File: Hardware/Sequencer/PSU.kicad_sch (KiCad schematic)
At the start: 1 part, among them U601 AZ1117H-ADJ

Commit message: Régu
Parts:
- added C1, C2: 33nF, symbol Device:C
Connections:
- net GND: now also C1.2, C2.2

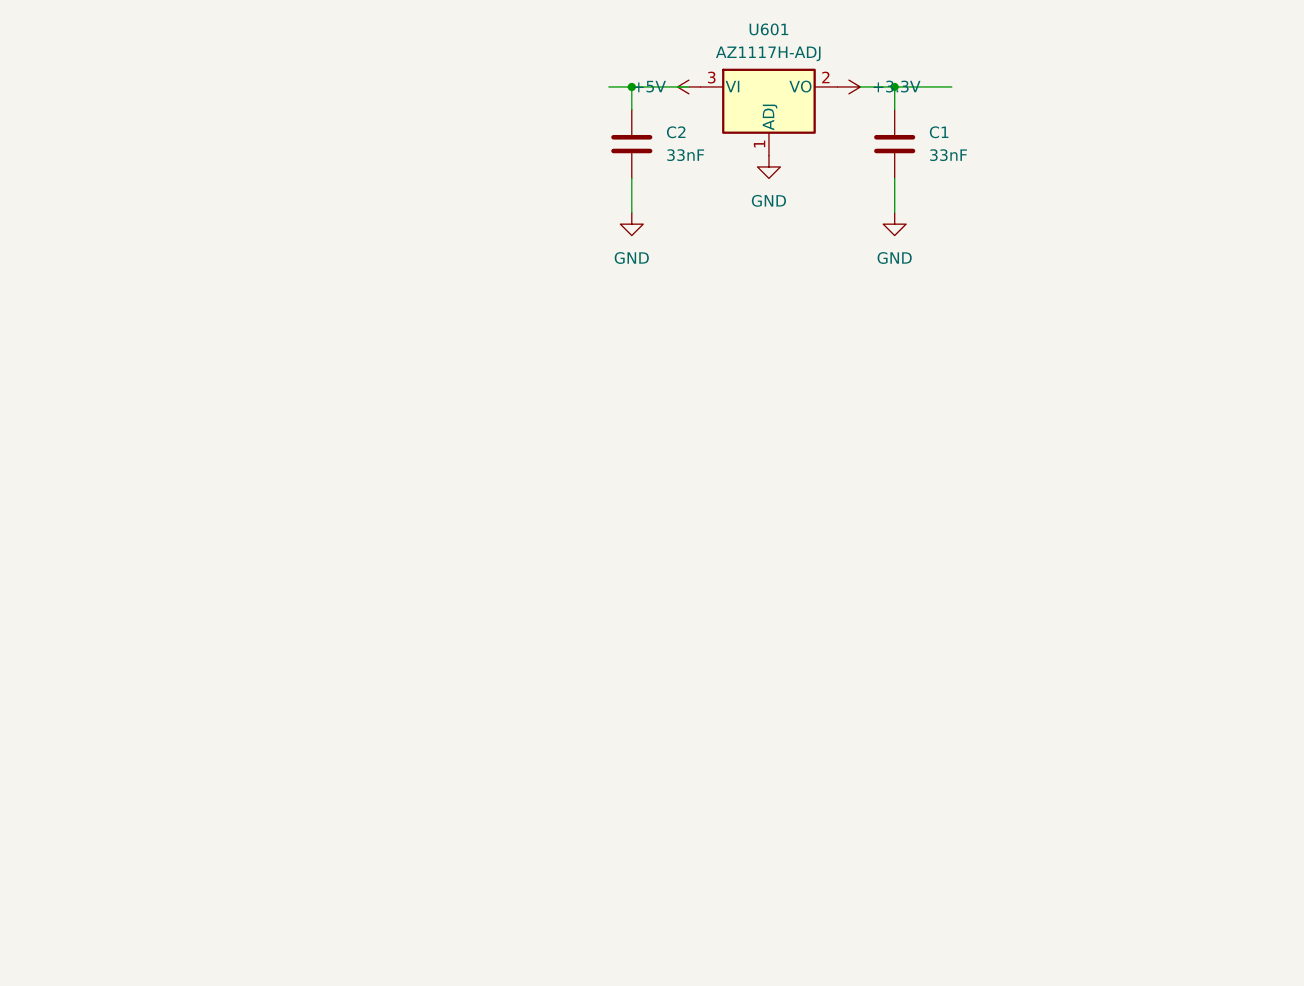
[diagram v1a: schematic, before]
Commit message: Beaucoup de changements sur le pcb
Alim corrigée, ajout de l'USB C

Sonde sur le processeur + linkage USB

Rajout des boutons (465M111...)
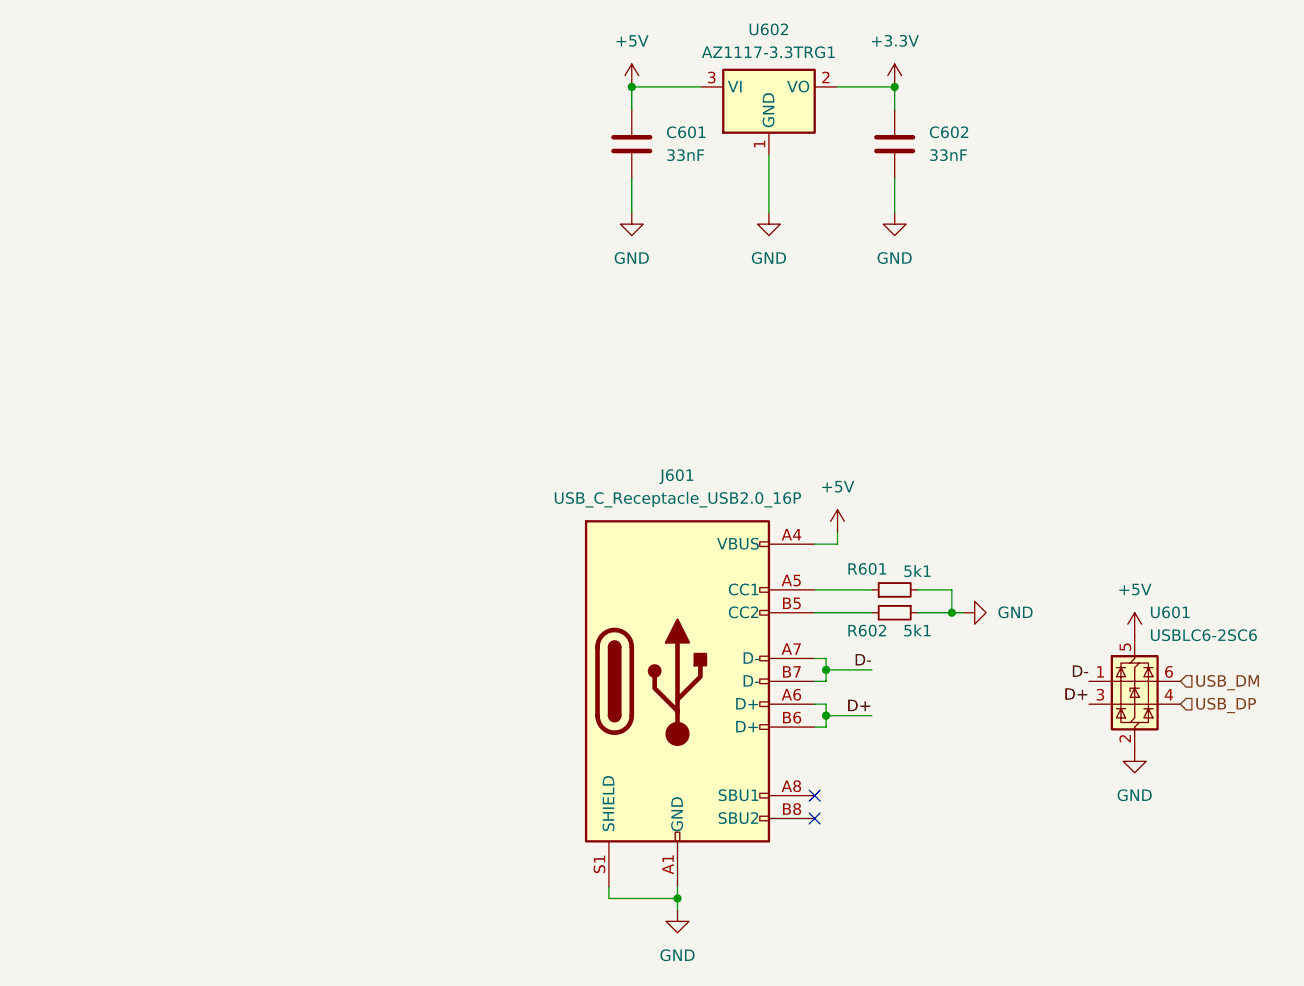
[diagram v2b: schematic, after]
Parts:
- removed U601: AZ1117H-ADJ, Package_TO_SOT_SMD:SOT-223-3_TabPin2, symbol Regulator_Linear:AZ1117H-ADJ
- added J601: USB_C_Receptacle_USB2.0_16P, Connector_USB:USB_C_Receptacle_HRO_TYPE-C-31-M-12, symbol Connector:USB_C_Receptacle_USB2.0_16P
- added R601, R602: 5k1, symbol Device:R_Small
- added U601: USBLC6-2SC6, Package_TO_SOT_SMD:SOT-223-3_TabPin2, symbol Power_Protection:USBLC6-2SC6
- added U602: AZ1117-3.3TRG1, Package_TO_SOT_SMD:SOT-223-3_TabPin2, symbol Regulator_Linear:AMS1117-3.3
- renumbered C2 to C601, C1 to C602
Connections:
- net +3.3V: now also C602.1, U602.2 (VO)
- net +5V: now also C601.1, J601.A4 (VBUS), J601.A9 (VBUS), J601.B4 (VBUS), J601.B9 (VBUS), U601.5 (VBUS), U602.3 (VI)
- net GND: now also J601.A1 (GND), J601.A12 (GND), J601.B1 (GND), J601.B12 (GND), J601.S1 (SHIELD), R601.2, R602.1, U601.2 (GND), U602.1 (GND)
- new net: J601.A5 (CC1), R601.1
- new net: J601.B5 (CC2), R602.2
- new net D+: J601.A6 (D+), J601.B6 (D+), U601.3 (I/O2)
- new net D-: J601.A7 (D-), J601.B7 (D-), U601.1 (I/O1)
- new net USB_DM: U601.6 (I/O1)
- new net USB_DP: U601.4 (I/O2)
- no-connect marks 0 -> 2

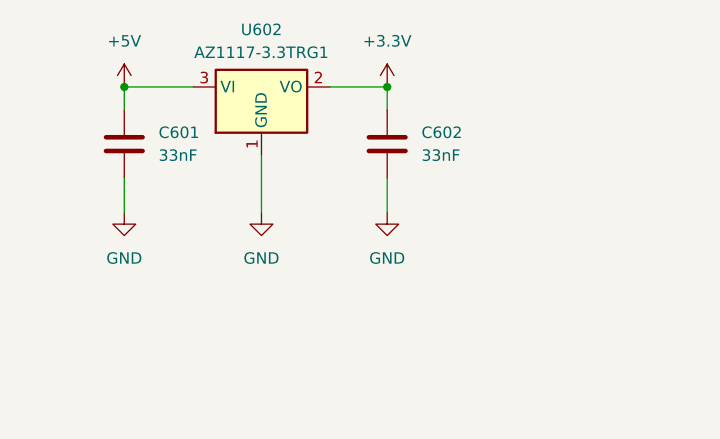
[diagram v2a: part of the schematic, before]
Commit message: update dimension pcb, footprint
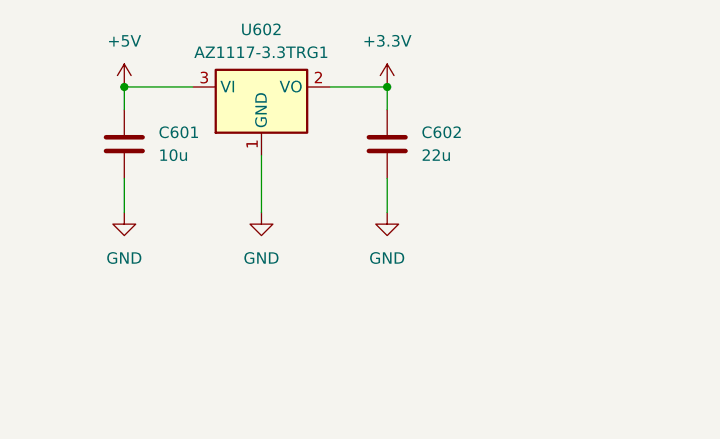
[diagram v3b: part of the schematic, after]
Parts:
- C601: value 33nF -> 10u; footprint (none) -> Capacitor_SMD:C_0603_1608Metric
- C602: value 33nF -> 22u; footprint (none) -> Capacitor_SMD:C_0603_1608Metric
- R601, R602: footprint (none) -> Resistor_SMD:R_0402_1005Metric
- U601: footprint Package_TO_SOT_SMD:SOT-223-3_TabPin2 -> Package_TO_SOT_SMD:SOT-23-6
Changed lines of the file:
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@@
 			)
 		)
-		(property "Footprint" "Package_TO_SOT_SMD:SOT-223-3_TabPin2"
+		(property "Footprint" "Package_TO_SOT_SMD:SOT-23-6"
 			(at 157.48 146.05 0)
 			(effects
@@
 			)
 		)
-		(property "Value" "33nF"
+		(property "Value" "10u"
 			(at 104.14 81.2799 0)
 			(effects
@@
 			)
 		)
-		(property "Footprint" ""
+		(property "Footprint" "Capacitor_SMD:C_0603_1608Metric"
 			(at 101.2952 83.82 0)
 			(effects
@@
 			)
 		)
-		(property "Footprint" ""
+		(property "Footprint" "Resistor_SMD:R_0402_1005Metric"
 			(at 129.54 132.08 0)
 			(effects
@@
 			)
 		)
-		(property "Value" "33nF"
+		(property "Value" "22u"
 			(at 133.35 81.2799 0)
 			(effects
@@
 			)
 		)
-		(property "Footprint" ""
+		(property "Footprint" "Capacitor_SMD:C_0603_1608Metric"
 			(at 130.5052 83.82 0)
 			(effects
@@
 			)
 		)
-		(property "Footprint" ""
+		(property "Footprint" "Resistor_SMD:R_0402_1005Metric"
 			(at 129.54 129.54 0)
 			(effects

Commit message: pcb
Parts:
- added SW1: SW_DIP_x01, symbol Switch:SW_DIP_x01
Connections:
- net +5V: now also SW1.1, SW1.2
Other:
- note added: "!!SWITCH FIND REF!!"
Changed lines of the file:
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@@
 		)
 	)
-	(label "D+"
-		(at 127 143.51 180)
-		(fields_autoplaced yes)
+	(text "!!SWITCH FIND REF!!\n"
+		(exclude_from_sim no)
+		(at 49.784 94.488 0)
 		(effects
 			(font
 				(size 1.27 1.27)
 			)
-			(justify right bottom)
-		)
-	)
-	(label "D-"
-		(at 127 138.43 180)
+		)
+	)
+	(label "D+"
+		(at 127 143.51 180)
 		(fields_autoplaced yes)
 		(effects
@@
 		)
 	)
-	(label "D+"
-		(at 151.13 142.24 180)
+	(label "D-"
+		(at 127 138.43 180)
 		(fields_autoplaced yes)
 		(effects
@@
 		)
 	)
-	(label "D-"
-		(at 151.13 139.7 180)
+	(label "D+"
+		(at 151.13 142.24 180)
 		(fields_autoplaced yes)
 		(effects
@@
 		)
 	)
+	(label "D-"
+		(at 151.13 139.7 180)
+		(fields_autoplaced yes)
+		(effects
+			(font
+				(size 1.27 1.27)
+			)
+			(justify right bottom)
+		)
+	)
 	(hierarchical_label "USB_DM"
 		(shape input)
@@
 	)
 	(symbol
+		(lib_id "power:+5V")
+		(at 55.88 106.68 270)
+		(unit 1)
+		(exclude_from_sim no)
+		(in_bom yes)
+		(on_board yes)
+		(dnp no)
+		(fields_autoplaced yes)
+		(property "Reference" "#PWR046"
+			(at 52.07 106.68 0)
+			(effects
+				(font
+					(size 1.27 1.27)
+				)
+				(hide yes)
+			)
+		)
+		(property "Value" "+5V"
+			(at 59.69 106.6799 90)
+			(effects
+				(font
+					(size 1.27 1.27)
+				)
+				(justify left)
+			)
+		)
+		(property "Footprint" ""
+			(at 55.88 106.68 0)
+			(effects
+				(font
+					(size 1.27 1.27)
+				)
+				(hide yes)
+			)
+		)
+		(property "Datasheet" ""
+			(at 55.88 106.68 0)
+			(effects
+				(font
+					(size 1.27 1.27)
+				)
+				(hide yes)
+			)
+		)
+		(property "Description" "Power symbol creates a global label with name \"+5V\""
+			(at 55.88 106.68 0)
+			(effects
+				(font
+					(size 1.27 1.27)
+				)
+				(hide yes)
+			)
+		)
+		(pin "1"
+		)
+		(instances
+			(project "Sequencer"
+				(path "/bb3f736c-029c-4f1c-9c8c-1e3d4a336366/3a3a9b01-b73b-4ccd-9cf4-ad4078db162d"
+					(reference "#PWR046")
+					(unit 1)
+				)
+			)
+		)
+	)
+	(symbol
+		(lib_id "Switch:SW_DIP_x01")
+		(at 48.26 106.68 0)
+		(unit 1)
+		(exclude_from_sim no)
+		(in_bom yes)
+		(on_board yes)
+		(dnp no)
+		(fields_autoplaced yes)
+		(property "Reference" "SW1"
+			(at 48.26 99.06 0)
+			(effects
+				(font
+					(size 1.27 1.27)
+				)
+			)
+		)
+		(property "Value" "SW_DIP_x01"
+			(at 48.26 101.6 0)
+			(effects
+				(font
+					(size 1.27 1.27)
+				)
+			)
+		)
+		(property "Footprint" ""
+			(at 48.26 106.68 0)
+			(effects
+				(font
+					(size 1.27 1.27)
+				)
+				(hide yes)
+			)
+		)
+		(property "Datasheet" "~"
+			(at 48.26 106.68 0)
+			(effects
+				(font
+					(size 1.27 1.27)
+				)
+				(hide yes)
+			)
+		)
+		(property "Description" "1x DIP Switch, Single Pole Single Throw (SPST) switch, small symbol"
+			(at 48.26 106.68 0)
+			(effects
+				(font
+					(size 1.27 1.27)
+				)
+				(hide yes)
+			)
+		)
+		(pin "1"
+		)
+		(pin "2"
+		)
+		(instances
+			(project "Sequencer"
+				(path "/bb3f736c-029c-4f1c-9c8c-1e3d4a336366/3a3a9b01-b73b-4ccd-9cf4-ad4078db162d"
+					(reference "SW1")
+					(unit 1)
+				)
+			)
+		)
+	)
+	(symbol
 		(lib_id "Power_Protection:USBLC6-2SC6")
 		(at 156.21 139.7 0)
@@
 					(unit 1)
 				)
+			)
+		)
+	)
+	(symbol
+		(lib_id "power:+5V")
+		(at 40.64 106.68 90)
+		(unit 1)
+		(exclude_from_sim no)
+		(in_bom yes)
+		(on_board yes)
+		(dnp no)
+		(fields_autoplaced yes)
+		(property "Reference" "#PWR045"
+			(at 44.45 106.68 0)
+			(effects
+				(font
+					(size 1.27 1.27)
+				)
+				(hide yes)
+			)
+		)
+		(property "Value" "+5V"
+			(at 36.83 106.6799 90)
+			(effects
+				(font
+					(size 1.27 1.27)
+				)
+				(justify left)
+			)
+		)
+		(property "Footprint" ""
+			(at 40.64 106.68 0)
+			(effects
+				(font
+					(size 1.27 1.27)
+				)
+				(hide yes)
+			)
+		)
+		(property "Datasheet" ""
+			(at 40.64 106.68 0)
+			(effects
+				(font
+					(size 1.27 1.27)
+				)
+				(hide yes)
+			)
+		)
+		(property "Description" "Power symbol creates a global label with name \"+5V\""
+			(at 40.64 106.68 0)
+			(effects
+				(font
+					(size 1.27 1.27)
+				)
+				(hide yes)
+			)
+		)
+		(pin "1"
+		)
+		(instances
+			(project "Sequencer"
+				(path "/bb3f736c-029c-4f1c-9c8c-1e3d4a336366/3a3a9b01-b73b-4ccd-9cf4-ad4078db162d"
+					(reference "#PWR045")
+					(unit 1)
+				)

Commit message: update pcb
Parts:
- removed SW1: SW_DIP_x01, symbol Switch:SW_DIP_x01
- added SW601: SW_SPDT, Library:472121010111, symbol Switch:SW_SPDT
- renumbered U602 to U601, U601 to U602
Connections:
- net +5V: now also SW601.2 (B); no longer J601.A4 (VBUS), J601.A9 (VBUS), J601.B4 (VBUS), J601.B9 (VBUS), U602.5 (VBUS)
- net GND: now also SW601.3 (C)
- new net VBUS: J601.A4 (VBUS), J601.A9 (VBUS), J601.B4 (VBUS), J601.B9 (VBUS), SW601.1 (A), U602.5 (VBUS)
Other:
- note removed: "!!SWITCH FIND REF!!"
